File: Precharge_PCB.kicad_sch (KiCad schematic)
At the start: 72 parts, among them J1 MolexMicrofitPlus, J10 Conn_01x06, J2 MolexMicrofitPlus, J3 Conn_01x08, J4 MolexMicrofitPlus, J5 MolexMicrofitPlus, J6 MolexMicrofitPlus, K1 G2RL-1A, K2 G2RL-1A, Q1 DMN61D8LQ, Q2 DMN61D8LQ, SW2 SW_Push, U1 SN65HVD1050D, U2 TPS7B88, U3 STM32F103C8Tx, U4 MCP1700x-330xxMB, Y1 8M

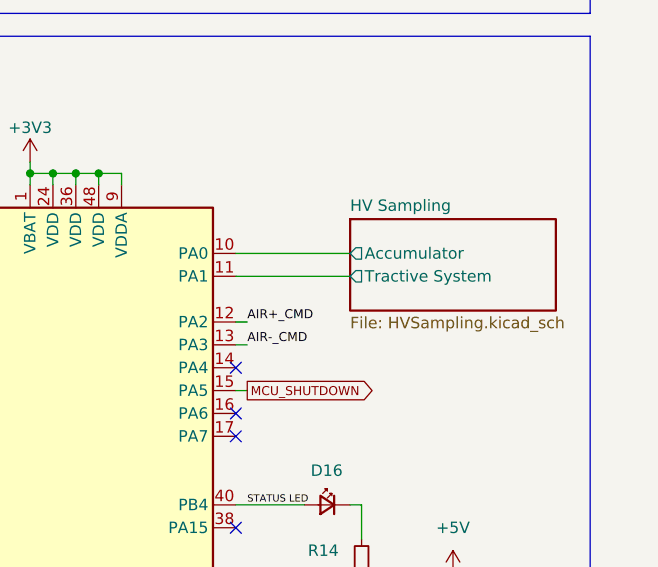
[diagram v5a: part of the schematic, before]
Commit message: schematic: Avoid using PA0 for analog sampling
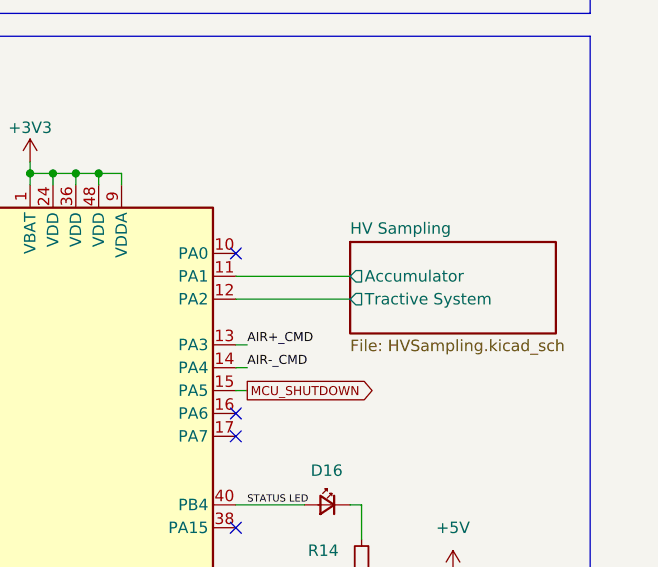
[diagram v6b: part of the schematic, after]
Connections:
- net AIR+_CMD: now also U3.13 (PA3); no longer U3.12 (PA2)
- net AIR-_CMD: now also U3.14 (PA4); no longer U3.13 (PA3)
- net HV Sampling/Accumulator: now also U3.11 (PA1); no longer U3.10 (PA0)
- net HV Sampling/Tractive System: now also U3.12 (PA2); no longer U3.11 (PA1)
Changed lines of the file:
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@@
 	)
 	(no_connect
-		(at 243.84 90.17)
-	)
-	(no_connect
 		(at 243.84 95.25)
 	)
@@
 	)
 	(no_connect
+		(at 243.84 77.47)
+	)
+	(no_connect
 		(at 243.84 138.43)
 	)
@@
 	(wire
 		(pts
-			(xy 243.84 85.09) (xy 245.11 85.09)
+			(xy 243.84 87.63) (xy 245.11 87.63)
 		)
 		(stroke
@@
 	(wire
 		(pts
-			(xy 243.84 77.47) (xy 256.54 77.47)
-		)
-		(stroke
-			(width 0)
-			(type default)
-		)
-	)
-	(wire
-		(pts
 			(xy 181.61 76.2) (xy 172.72 76.2)
 		)
@@
 	(wire
 		(pts
+			(xy 243.84 82.55) (xy 256.54 82.55)
+		)
+		(stroke
+			(width 0)
+			(type default)
+		)
+	)
+	(wire
+		(pts
 			(xy 27.94 123.19) (xy 29.21 123.19)
 		)
@@
 	(wire
 		(pts
-			(xy 243.84 87.63) (xy 245.11 87.63)
-		)
-		(stroke
-			(width 0)
-			(type default)
-		)
-	)
-	(wire
-		(pts
 			(xy 118.11 104.14) (xy 118.11 105.41)
 		)
@@
 	(wire
 		(pts
-			(xy 196.85 125.73) (xy 208.28 125.73)
+			(xy 243.84 80.01) (xy 256.54 80.01)
 		)
 		(stroke
@@
 	(wire
 		(pts
-			(xy 234.95 30.48) (xy 234.95 31.75)
+			(xy 196.85 125.73) (xy 208.28 125.73)
 		)
 		(stroke
@@
 	(wire
 		(pts
-			(xy 31.75 101.6) (xy 34.29 101.6)
+			(xy 234.95 30.48) (xy 234.95 31.75)
 		)
 		(stroke
@@
 	(wire
 		(pts
-			(xy 243.84 80.01) (xy 256.54 80.01)
+			(xy 31.75 101.6) (xy 34.29 101.6)
 		)
 		(stroke
@@
 	(wire
 		(pts
+			(xy 243.84 90.17) (xy 245.11 90.17)
+		)
+		(stroke
+			(width 0)
+			(type default)
+		)
+	)
+	(wire
+		(pts
 			(xy 139.7 133.35) (xy 138.43 133.35)
 		)
@@
 	)
 	(label "AIR-_CMD"
-		(at 245.11 87.63 0)
+		(at 245.11 90.17 0)
 		(effects
 			(font
@@
 	)
 	(label "AIR+_CMD"
-		(at 245.11 85.09 0)
+		(at 245.11 87.63 0)
 		(effects
 			(font
@@
 	)
 	(sheet
-		(at 256.54 73.66)
+		(at 256.54 76.2)
 		(size 22.86 10.16)
 		(exclude_from_sim no)
@@
 		)
 		(property "Sheetname" "HV Sampling"
-			(at 256.54 72.8996 0)
+			(at 256.54 75.4396 0)
 			(effects
 				(font
@@
 		)
 		(property "Sheetfile" "HVSampling.kicad_sch"
-			(at 256.54 84.4534 0)
+			(at 256.54 86.9934 0)
 			(effects
 				(font
@@
 		)
 		(pin "Accumulator" output
-			(at 256.54 77.47 180)
+			(at 256.54 80.01 180)
 			(effects
 				(font
@@
 		)
 		(pin "Tractive System" output
-			(at 256.54 80.01 180)
+			(at 256.54 82.55 180)
 			(effects
 				(font

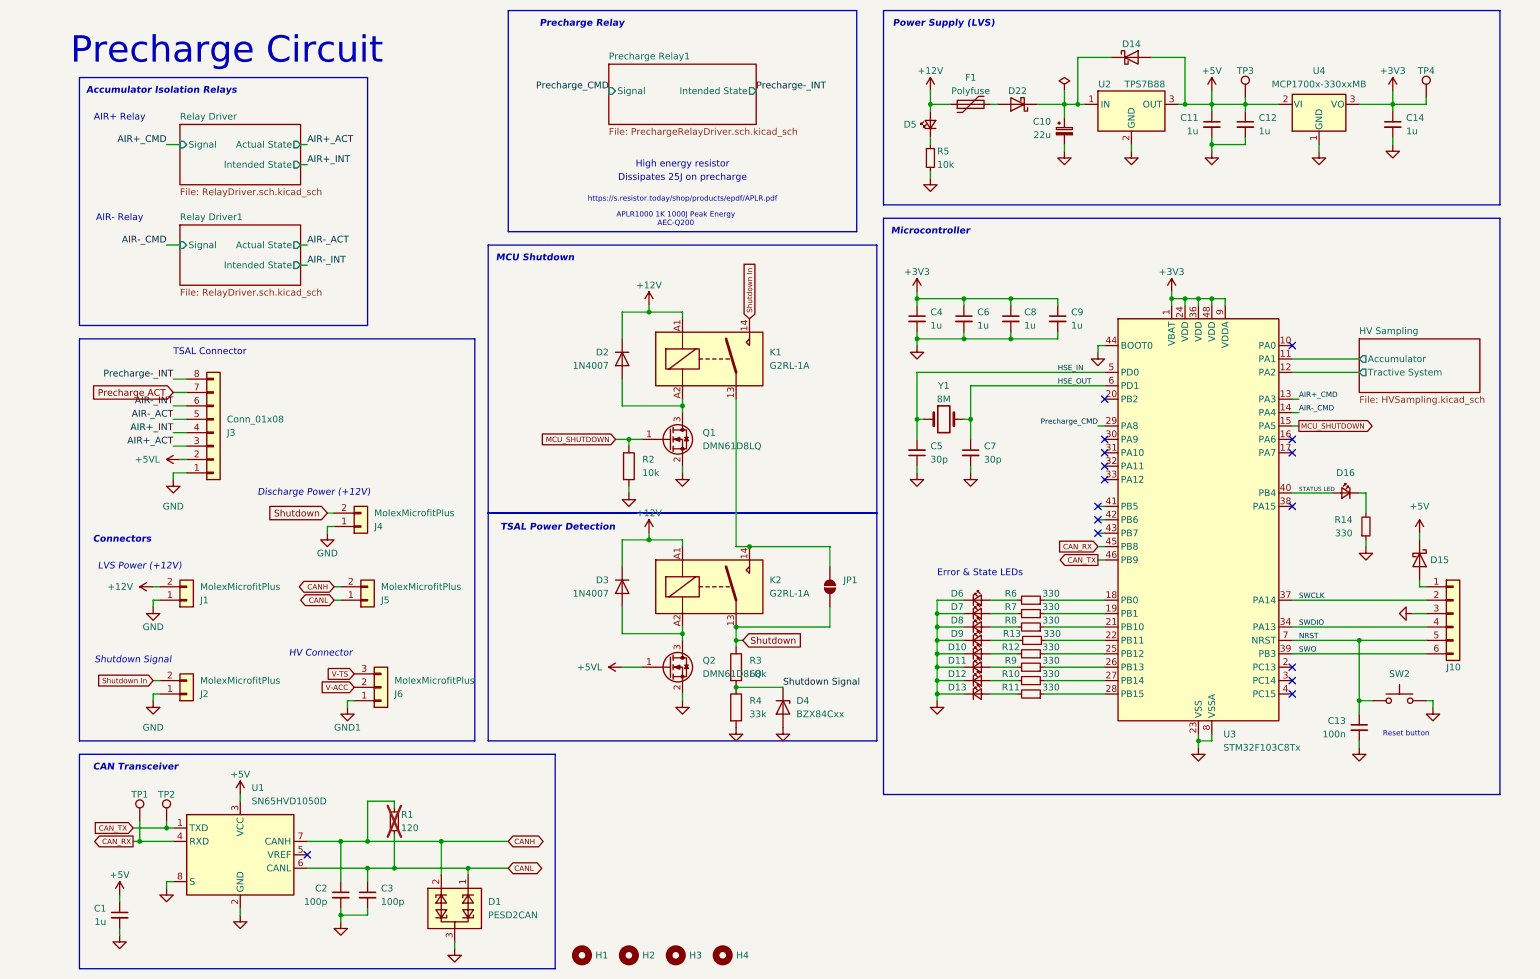
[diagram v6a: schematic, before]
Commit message: schematic: Cleanup all global labels
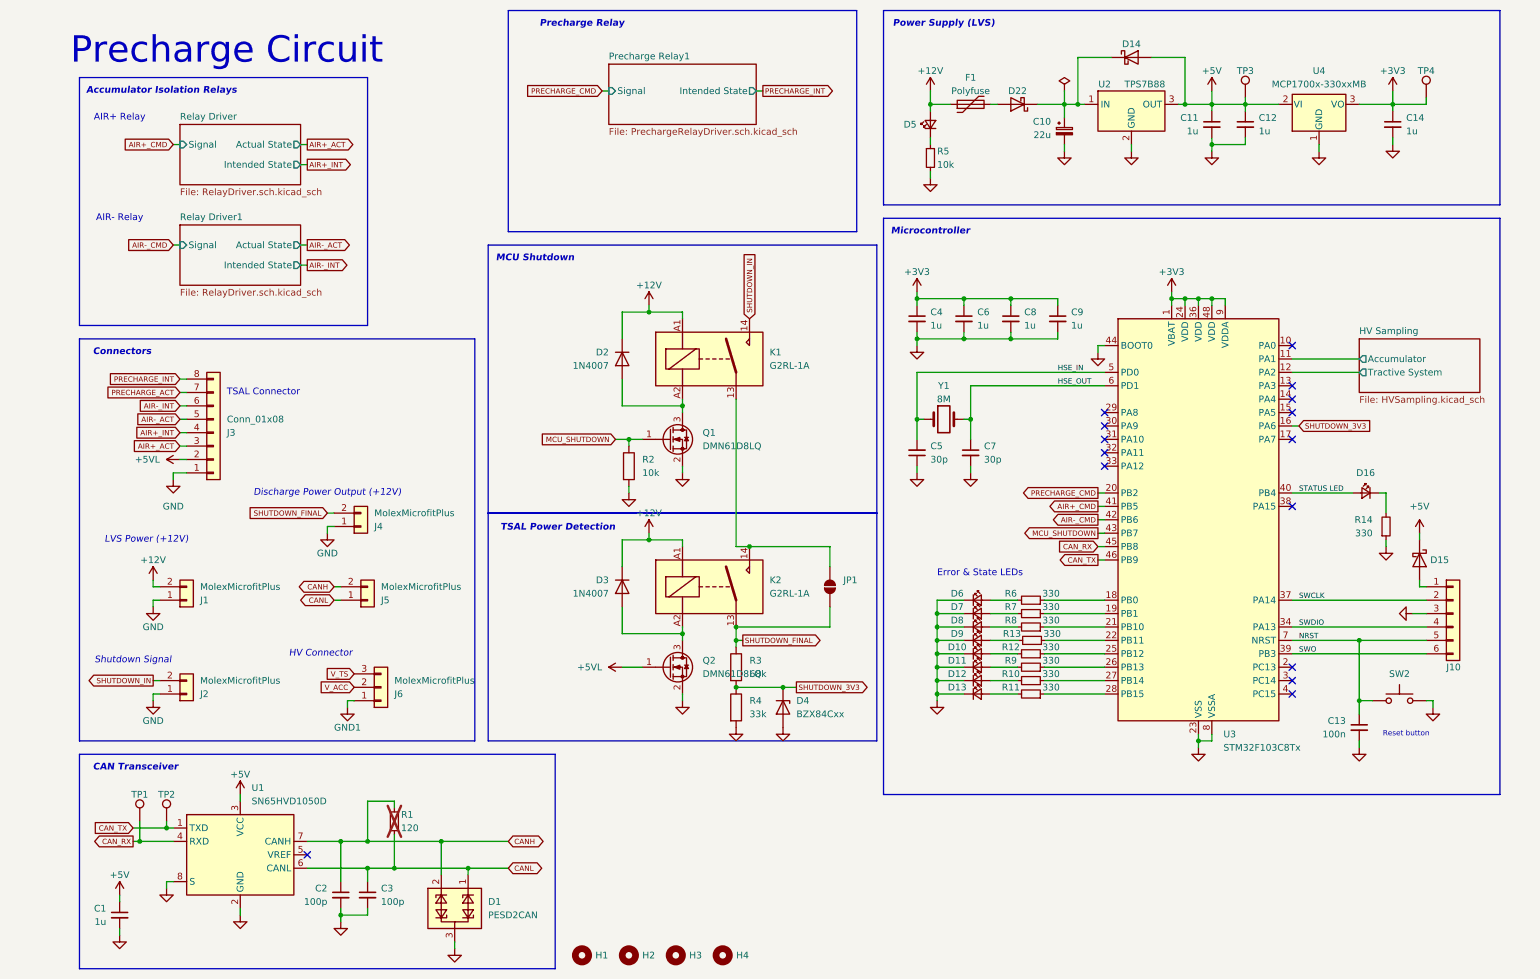
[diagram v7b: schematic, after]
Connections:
- net Shutdown Signal is gone; now on net SHUTDOWN_3V3: D4.3 (K), R3.2, R4.1
- net AIR+_CMD: now also U3.41 (PB5); no longer U3.13 (PA3)
- net AIR-_CMD: now also U3.42 (PB6); no longer U3.14 (PA4)
- net MCU_SHUTDOWN: now also U3.43 (PB7); no longer U3.15 (PA5)
- net SHUTDOWN_3V3: now reaches U3.16 (PA6)
- net PRECHARGE_CMD: now reaches U3.20 (PB2)
- net Precharge ACT renamed PRECHARGE_ACT
- net Precharge-_INT renamed PRECHARGE_INT
- net Precharge_CMD: no longer names the net of U3.29 (PA8)
- net Shutdown renamed SHUTDOWN_FINAL
- net Shutdown In renamed SHUTDOWN_IN
- net V-ACC renamed V_ACC
- net V-TS renamed V_TS
- no-connect marks 16 -> 15
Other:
- note added: "Discharge Power Output (+12V)"
- note removed: "APLR1000 1K 1000J Peak Energy AEC-Q200"
- note removed: "Discharge Power (+12V)"
- note removed: "Dissipates 25J on precharge"
- note removed: "High energy resistor"
- note removed: "https://s.resistor.today/shop/products/epdf/APLR.pdf"
- moved on the sheet: D16, R14

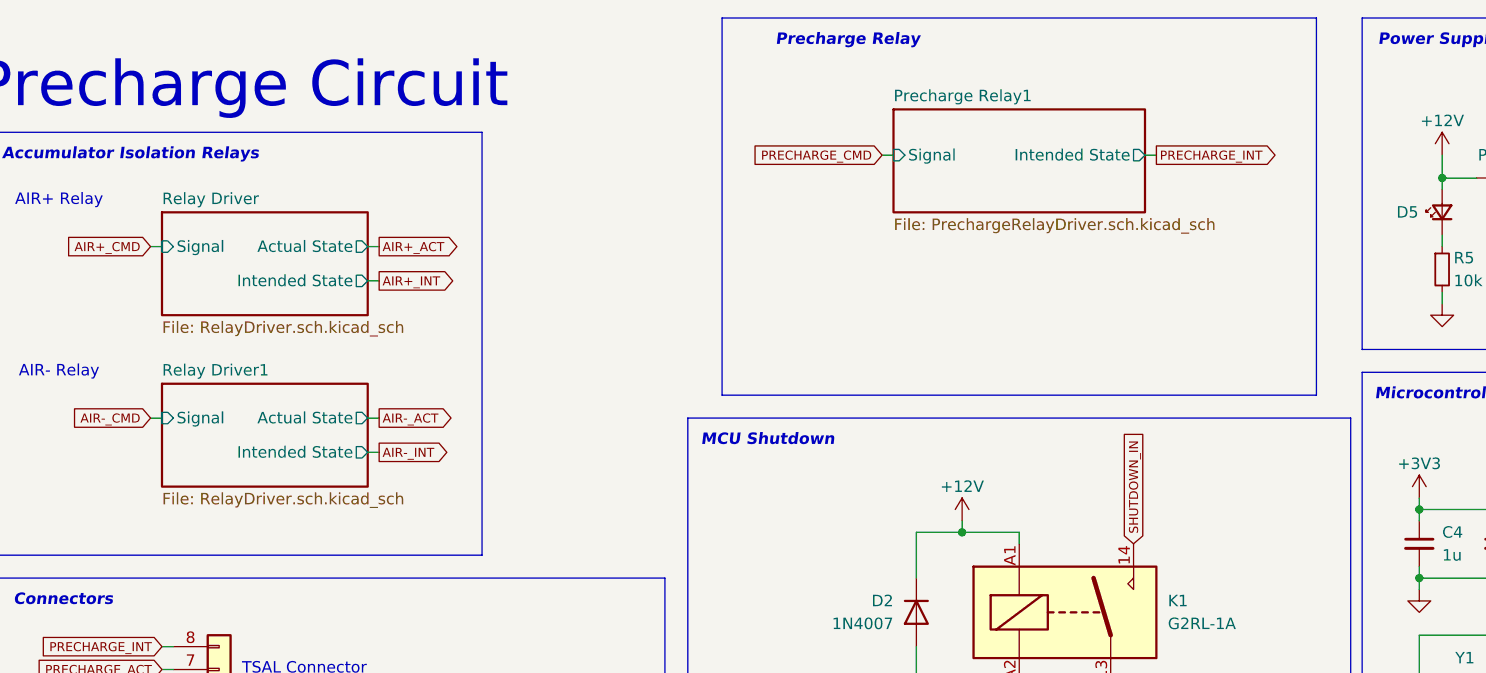
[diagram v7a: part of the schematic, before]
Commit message: schematic: Rename hierarchical sheets
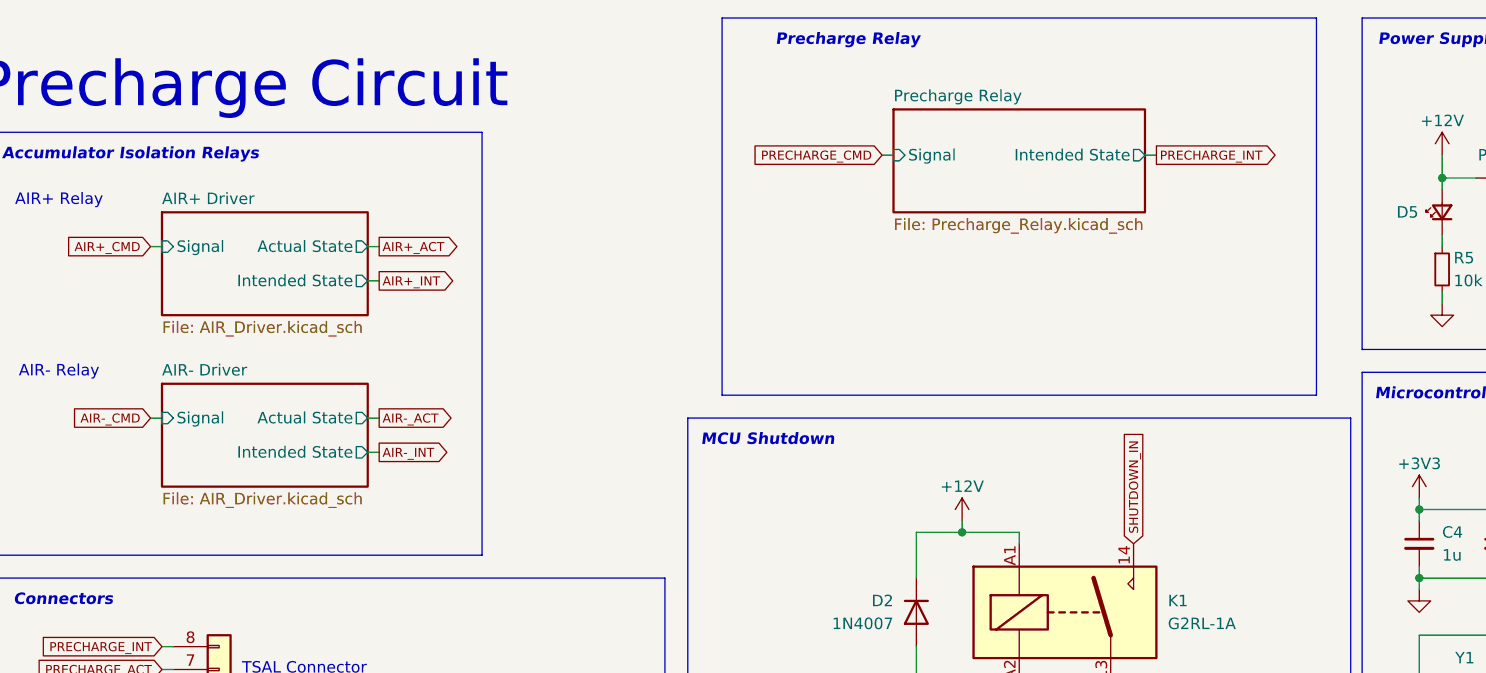
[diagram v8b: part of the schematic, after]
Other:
- sheet Precharge Relay1 renamed Precharge Relay
- sheet Relay Driver renamed AIR+ Driver
- removed sheet Relay Driver1
- added sheet AIR- Driver (AIR_Driver.kicad_sch)
- sheet AIR+ Driver: file RelayDriver.sch.kicad_sch -> AIR_Driver.kicad_sch
- sheet Precharge Relay: file PrechargeRelayDriver.sch.kicad_sch -> Precharge_Relay.kicad_sch
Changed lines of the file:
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@@
 			(color 0 0 0 0.0000)
 		)
-		(property "Sheetname" "Relay Driver1"
+		(property "Sheetname" "AIR- Driver"
 			(at 33.02 53.8496 0)
 			(effects
@@
 			)
 		)
-		(property "Sheetfile" "RelayDriver.sch.kicad_sch"
+		(property "Sheetfile" "AIR_Driver.kicad_sch"
 			(at 33.02 66.6734 0)
 			(effects
@@
 			(color 0 0 0 0.0000)
 		)
-		(property "Sheetname" "Relay Driver"
+		(property "Sheetname" "AIR+ Driver"
 			(at 33.02 34.7996 0)
 			(effects
@@
 			)
 		)
-		(property "Sheetfile" "RelayDriver.sch.kicad_sch"
+		(property "Sheetfile" "AIR_Driver.kicad_sch"
 			(at 33.02 47.6234 0)
 			(effects
@@
 			(color 0 0 0 0.0000)
 		)
-		(property "Sheetname" "Precharge Relay1"
+		(property "Sheetname" "Precharge Relay"
 			(at 114.3 23.3696 0)
 			(effects
@@
 			)
 		)
-		(property "Sheetfile" "PrechargeRelayDriver.sch.kicad_sch"
+		(property "Sheetfile" "Precharge_Relay.kicad_sch"
 			(at 114.3 36.1934 0)
 			(effects
